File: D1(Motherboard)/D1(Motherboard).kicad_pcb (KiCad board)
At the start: 4 copper layers, 38 x 35 mm, 73 parts, among them J1 WR-FPC_0.5mm_ZIF_V, J2 USB_C_Receptacle_USB2.0, J3 B2B-PH-K-S, Q1 NX2301P.215, SW1 CHS-02A, U1 ESP32-S2, U2 ICM-20602, U3 WR-FPC_0.5mm_ZIF_H, U4 MIC5353-3.3YMT, U5 FAN5331SX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

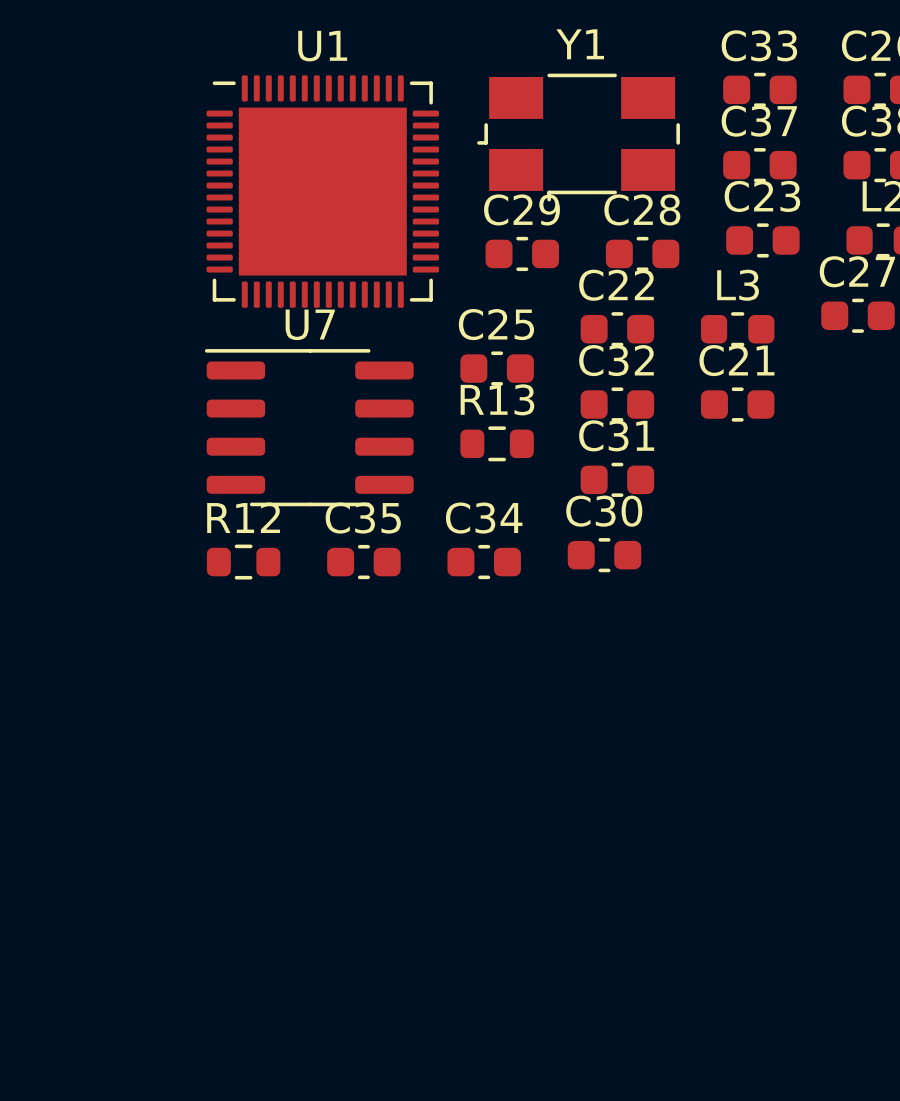
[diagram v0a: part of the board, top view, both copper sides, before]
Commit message: Added Flash memory, is it worth adding PSRAM???
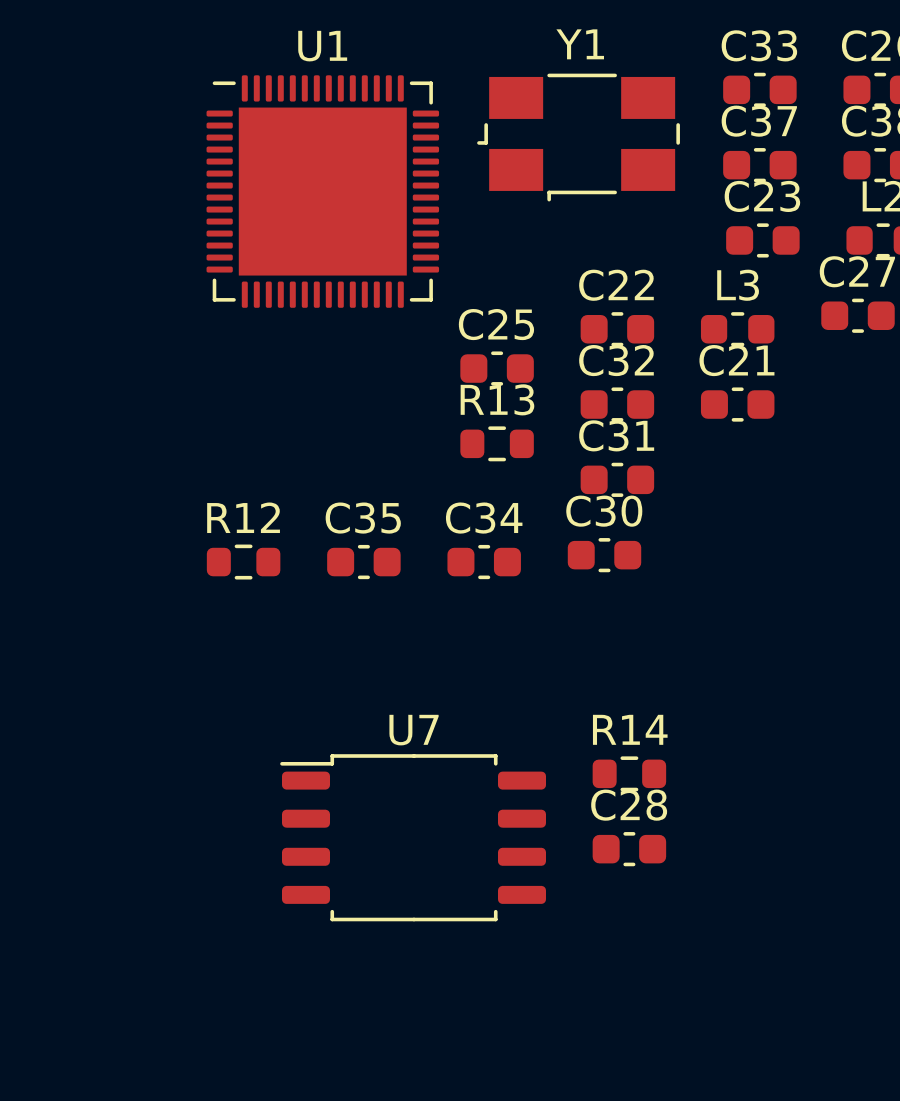
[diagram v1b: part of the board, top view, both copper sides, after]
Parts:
- removed C29: 270p, Capacitor_SMD:C_0603_1608Metric
- added R14: 10k(NC), Resistor_SMD:R_0603_1608Metric, F.Cu at (100.9, 59.5)
- C28: value 270p -> 0.1u
- U7: value AT25SF081-SSHD-X -> W25Q128JVS; footprint Package_SO:SOIC-8_3.9x4.9mm_P1.27mm -> Package_SO:SOIC-8_5.23x5.23mm_P1.27mm
- moved C28 19.8 mm to (100.9, 62.0)
- moved U7 14.1 mm to (93.7, 61.7)
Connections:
- net SHD/SD2 renamed SPIHD
- net SWP/SD3 renamed SPIWP
- C28 pad 1: unconnected-(C28-Pad1) -> VDD_SPI
- C28 pad 2: unconnected-(C28-Pad2) -> GND
- R13 pad 1: unconnected-(R13-Pad1) -> Net-(R13-Pad1)
- R13 pad 2: unconnected-(R13-Pad2) -> U0TXD
- U1 pad 33: SCS/CMD -> SPICS0
- U1 pad 34: SCK/CLK -> SPICLK
- U1 pad 35: SDI/SD1 -> SPIQ
- U1 pad 36: SDO/SD0 -> SPID
- U1 pad 48: unconnected-(U1-Pad48) -> Net-(R13-Pad1)
- U1 pad 49: unconnected-(U1-Pad49) -> U0RXD
- U7 pad 1: SCS/CMD -> SPICS0
- U7 pad 2: SDO/SD0 -> SPIQ
- U7 pad 5: SDI/SD1 -> SPID
- U7 pad 6: SCK/CLK -> SPICS0
- U7 pad 8: VDD_SDIO -> VDD_SPI

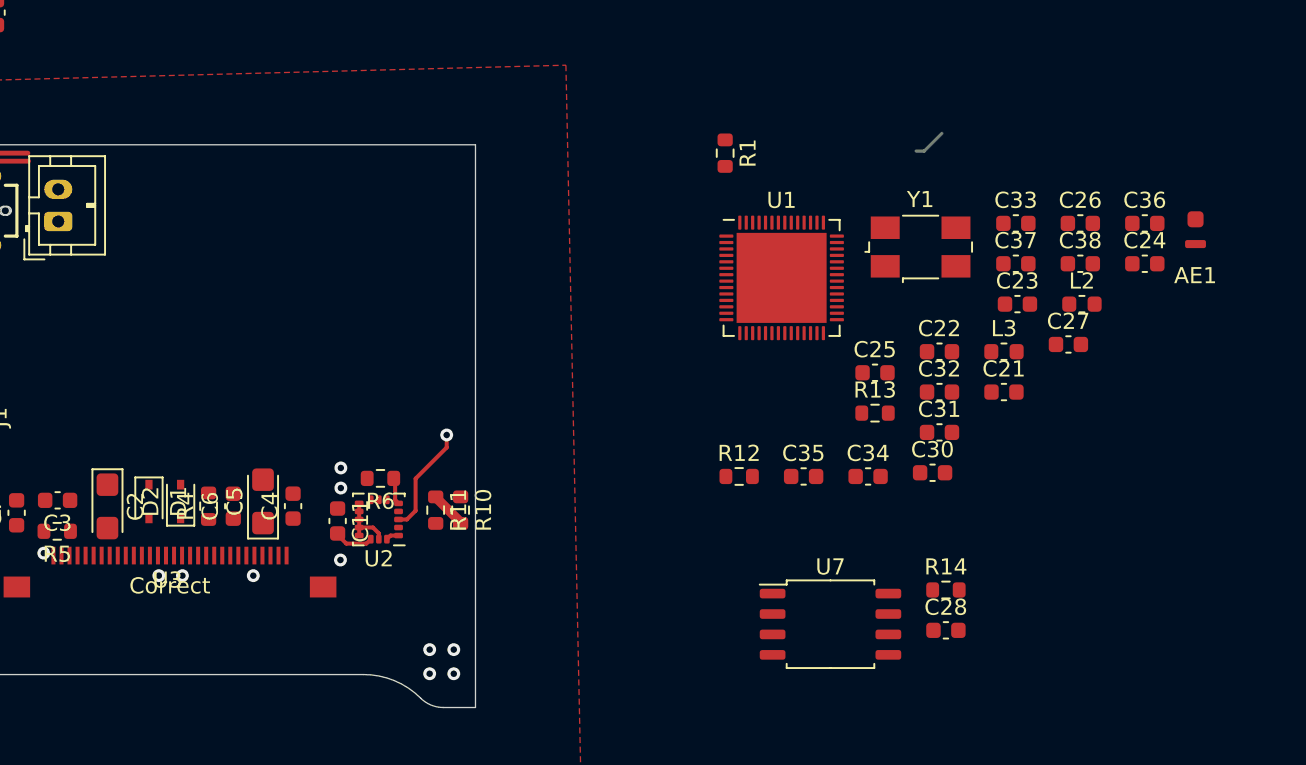
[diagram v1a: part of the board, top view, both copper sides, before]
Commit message: Sorted out antenna + setout loctions in corner
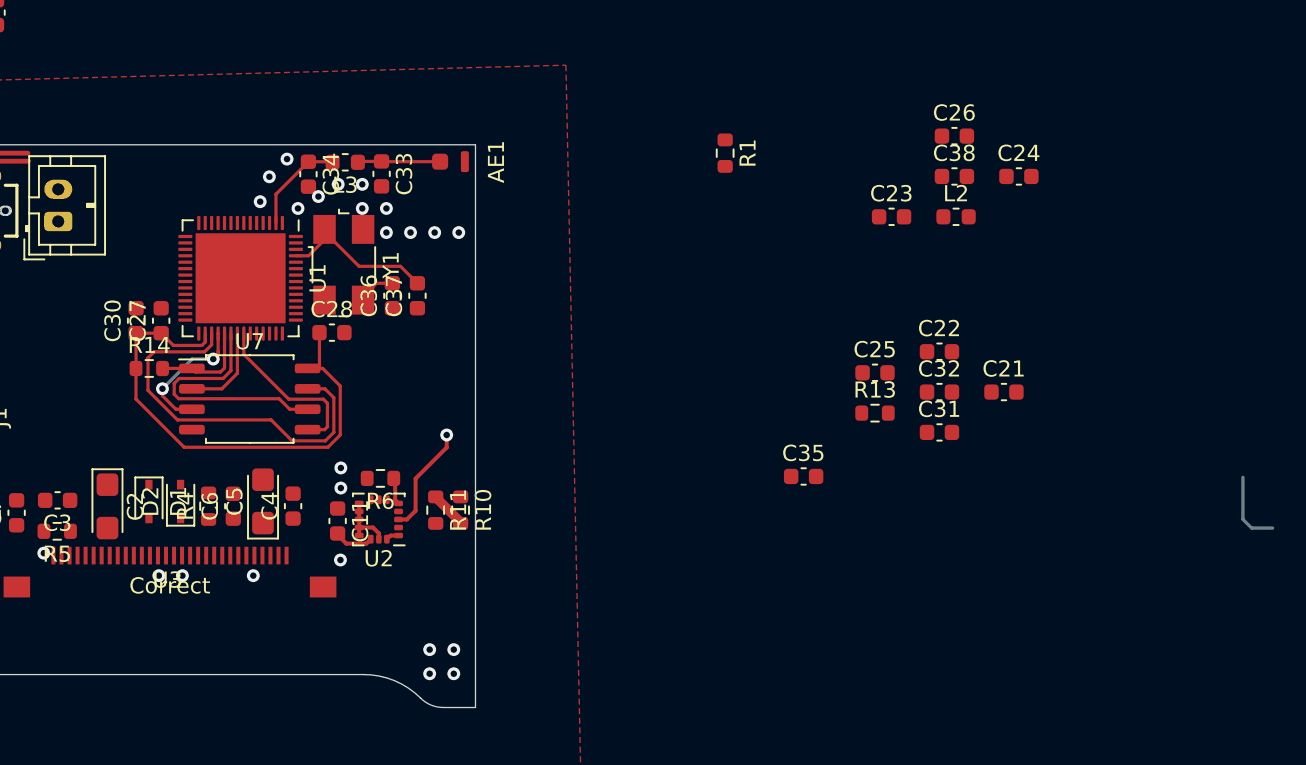
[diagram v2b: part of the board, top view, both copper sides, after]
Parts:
- removed R12: 0R, Resistor_SMD:R_0603_1608Metric
- moved C27 56.4 mm to (52.1, 42.8), turned to 90 degrees
- moved R14 51.4 mm to (51.3, 45.7)
- moved C30 50.4 mm to (50.5, 42.8), turned to 90 degrees
- moved C36 47.0 mm to (66.5, 41.2), turned to 90 degrees
- moved AE1 46.4 mm to (70.2, 32.9), turned to 90 degrees
- moved L3 42.6 mm to (63.5, 32.9), turned to 180 degrees
- moved C28 42.4 mm to (62.7, 43.5)
- moved C33 39.6 mm to (65.8, 33.6), turned to -90 degrees
- moved C34 39.6 mm to (61.2, 33.7), turned to -90 degrees
- moved U7 38.7 mm to (57.6, 47.6)
- moved C37 37.3 mm to (68.0, 41.2), turned to 90 degrees
- moved Y1 35.9 mm to (63.4, 39.3), turned to -90 degrees
- moved U1 33.6 mm to (57.0, 40.1), turned to -90 degrees
- moved C23 9.53 mm to (97.5, 36.3)
- moved C24 9.53 mm to (105.4, 33.8)
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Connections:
- C37 pad 2: Net-(C37-Pad2) -> XTAL_P
- U7 pad 6: SPICS0 -> SPICLK
- Y1 pad 1: Net-(C37-Pad2) -> XTAL_P
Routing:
- net VDD_SPI: track 0.00 -> 32.0 mm
- net SPIHD: track 0.00 -> 24.1 mm
- net SPICLK: track 0.00 -> 15.5 mm
- net SPIWP: track 0.00 -> 12.9 mm, vias 0 -> 2
- net SPID: track 0.00 -> 10.5 mm
- net XTAL_P: track 0.00 -> 10.1 mm
- net SPICS0: track 0.00 -> 6.20 mm
- net LNA_IN: track 0.00 -> 6.16 mm
- net SPIQ: track 0.00 -> 5.70 mm
- net Net-(AE1-Pad2): track 0.00 -> 5.14 mm
- net XTAL_N: track 0.00 -> 2.39 mm
- net (no net): track 2.06 -> 0.00 mm
- net GND: vias 11 -> 24

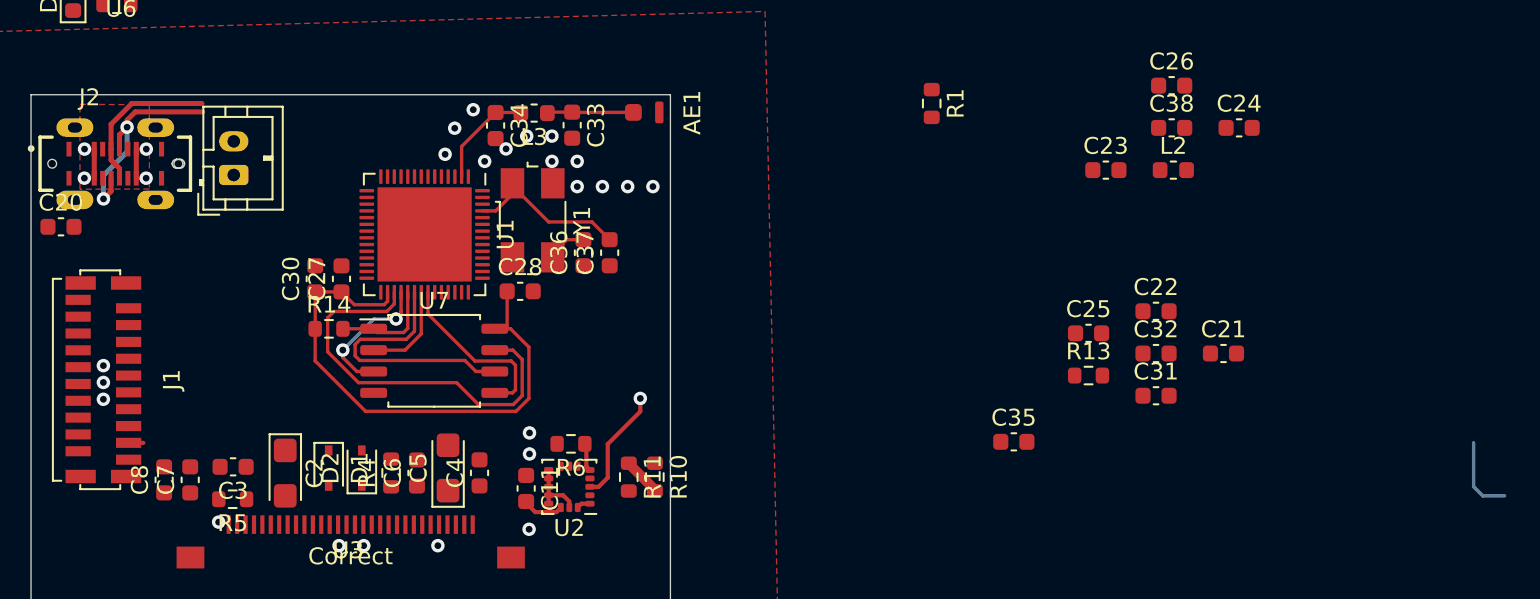
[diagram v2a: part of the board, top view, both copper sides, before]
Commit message: Fixed 3D Models etc, and added to schematics + PCB
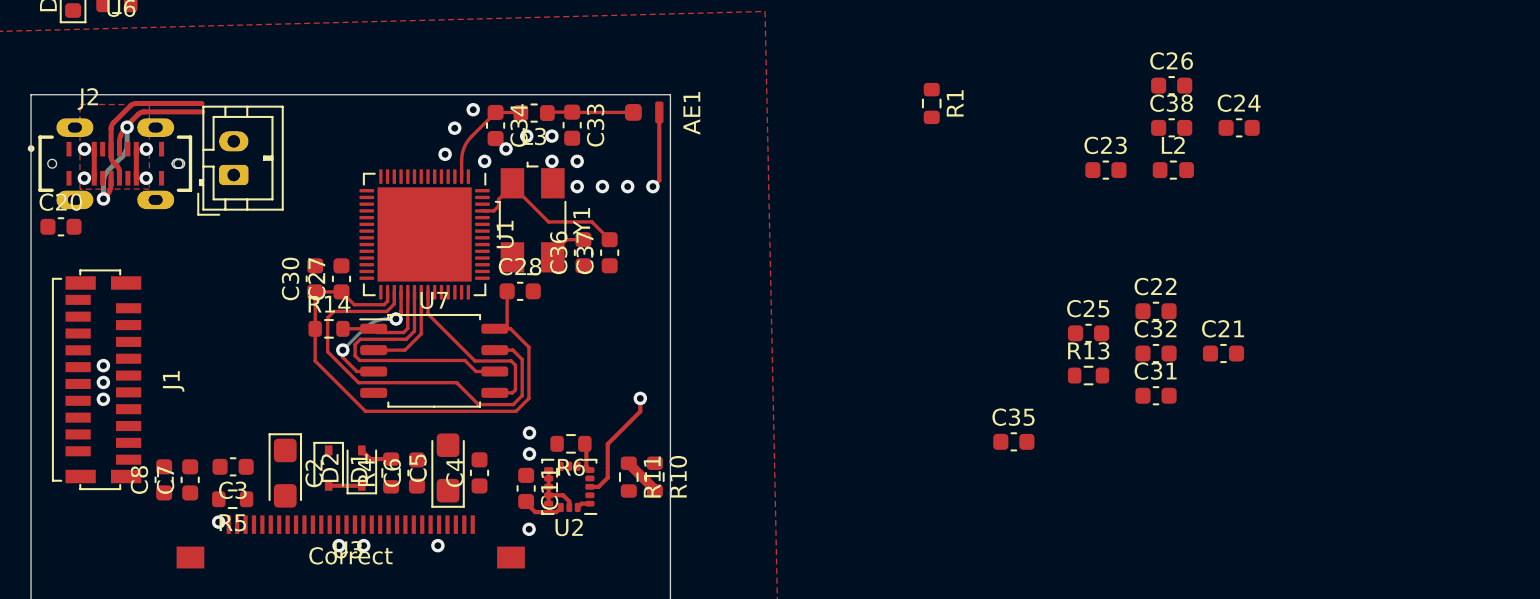
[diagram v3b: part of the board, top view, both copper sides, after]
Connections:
- U1 pad 25: unconnected-(U1-Pad25) -> D-
- U1 pad 26: unconnected-(U1-Pad26) -> D+
- U1 pad 39: unconnected-(U1-Pad39) -> MOSI
- U1 pad 40: unconnected-(U1-Pad40) -> CLK
- U1 pad 41: unconnected-(U1-Pad41) -> MISO
- U1 pad 5: unconnected-(U1-Pad5) -> Boot
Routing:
- net SPIWP: track 12.9 -> 8.16 mm
- net GND: track 9.14 -> 13.7 mm
- net Net-(D1-Pad2): track 0.00 -> 1.97 mm
- net Net-(D2-Pad2): track 0.00 -> 1.95 mm
- net MOSI: track 7.67 -> 6.80 mm

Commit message: More PCB work
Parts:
- removed C3: 1u, Capacitor_SMD:C_0603_1608Metric
- C2: value 100u -> 0.1u; footprint Capacitor_Tantalum_SMD:CP_EIA-3216-18_Kemet-A -> Capacitor_SMD:C_0603_1608Metric
- moved C24 50.5 mm to (55.0, 33.6), turned to 90 degrees
- moved C22 50.1 mm to (51.6, 33.6), turned to 90 degrees
- moved C25 49.2 mm to (47.4, 42.8), turned to -90 degrees
- moved L2 45.0 mm to (56.6, 33.6), turned to -90 degrees
- moved C23 44.3 mm to (53.3, 33.6), turned to 90 degrees
- moved C26 43.2 mm to (58.3, 33.6), turned to 90 degrees
- moved C21 42.0 mm to (62.9, 41.9)
- moved C31 38.8 mm to (62.9, 40.4)
- moved C32 38.6 mm to (62.9, 38.3)
- moved C35 33.1 mm to (62.9, 36.7)
- moved R11 28.4 mm to (50.0, 33.6), turned to 90 degrees
- moved U4 27.7 mm to (96.5, 56.3)
- moved D4 27.7 mm to (82.7, 58.2)
- moved C10 27.7 mm to (96.2, 59.3)
- moved C15 27.7 mm to (94.6, 56.2)
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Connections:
- C10 pad 2: VDD3P3_CPU -> +3V3
- C17 pad 2: VDD3P3_CPU -> +3V3
- C2 pad 1: VDD3P3_CPU -> +3V3
- C21 pad 1: VDD3P3_CPU -> +3V3
- C22 pad 1: VDD3P3_CPU -> +3V3
- C23 pad 1: VDD3P3_CPU -> +3V3
- C24 pad 1: VDD3P3_CPU -> +3V3
- C25 pad 1: VDD3P3_CPU -> +3V3
- C31 pad 1: VDD3P3_CPU -> +3V3
- C32 pad 1: VDD3P3_CPU -> +3V3
- C35 pad 1: VDD3P3_CPU -> +3V3
- C6 pad 1: VDD3P3_CPU -> +3V3
- C9 pad 2: VDD3P3_CPU -> +3V3
- J1 pad 11: VDD3P3_CPU -> +3V3
- J1 pad 13: VDD3P3_CPU -> +3V3
- J1 pad 9: VDD3P3_CPU -> +3V3
- L2 pad 1: VDD3P3_CPU -> +3V3
- R1 pad 1: VDD3P3_CPU -> +3V3
- U1 pad 1: VDD3P3_CPU -> +3V3
- U1 pad 14: unconnected-(U1-Pad14) -> Display1_CS
- U1 pad 15: unconnected-(U1-Pad15) -> Display2_CS
- U1 pad 16: unconnected-(U1-Pad16) -> Display3_CS
- U1 pad 17: unconnected-(U1-Pad17) -> Display4_CS
- U1 pad 18: unconnected-(U1-Pad18) -> Display5_CS
- U1 pad 19: unconnected-(U1-Pad19) -> Display6_CS
- U1 pad 20: VDD3P3_CPU -> +3V3
- U1 pad 27: unconnected-(U1-Pad27) -> +3V3
- U1 pad 45: VDD3P3_CPU -> +3V3
- U1 pad 51: VDD3P3_CPU -> +3V3
- U1 pad 54: VDD3P3_CPU -> +3V3
- U2 pad 1: VDD3P3_CPU -> +3V3
- U2 pad 16: VDD3P3_CPU -> +3V3
- U3 pad 4: VDD3P3_CPU -> +3V3
- U4 pad 4: VDD3P3_CPU -> +3V3
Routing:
- net Display6_CS: track 0.00 -> 21.6 mm
- net Display5_CS: track 0.00 -> 21.4 mm
- net Display4_CS: track 0.00 -> 21.1 mm
- net Display3_CS: track 0.00 -> 20.9 mm
- net Display2_CS: track 0.00 -> 20.6 mm
- net +3V3: track 0.00 -> 13.5 mm, vias 0 -> 3
- net +BATT: track 0.00 -> 11.3 mm
- net VBUS: track 3.46 -> 14.1 mm
- net XTAL_N: track 2.39 -> 12.6 mm
- net Net-(D3-Pad1): track 0.00 -> 9.70 mm
- net Net-(R10-Pad2): track 2.19 -> 9.70 mm
- net Net-(D3-Pad2): track 0.00 -> 6.65 mm
- net VDD3P3_CPU: track 5.64 -> 0.00 mm, vias 3 -> 0
- net Net-(R2-Pad1): track 0.00 -> 4.97 mm
- net VDD3P3: track 0.00 -> 4.50 mm
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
